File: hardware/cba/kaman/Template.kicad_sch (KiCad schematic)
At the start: 0 parts

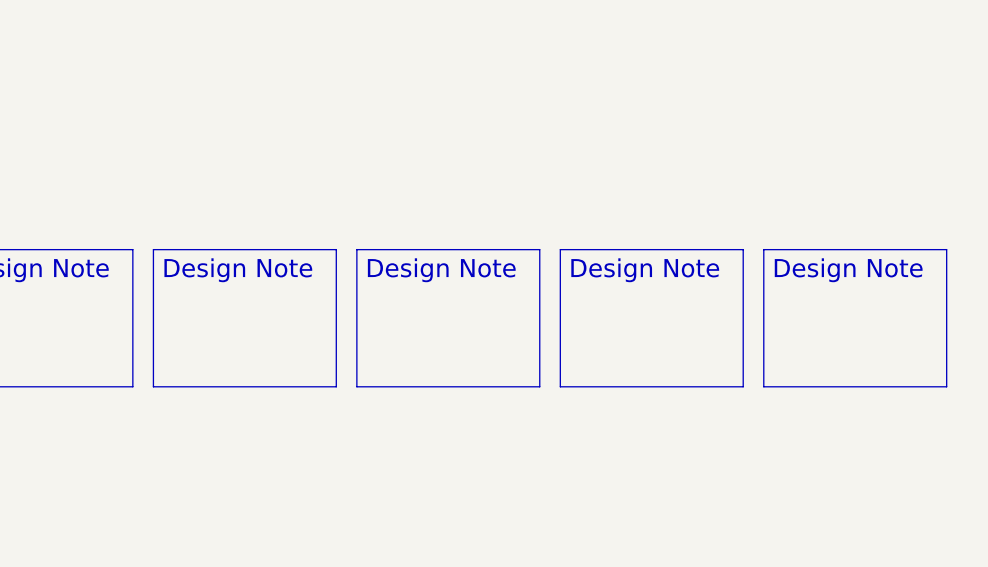
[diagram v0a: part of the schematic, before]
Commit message: hw(schematic): Draw the schematic part of ESP32 C6
Add the ESP32 C6 and it's necessary part's needed for it to function such as the decoupling caps, the auto program circuit and buttons needed
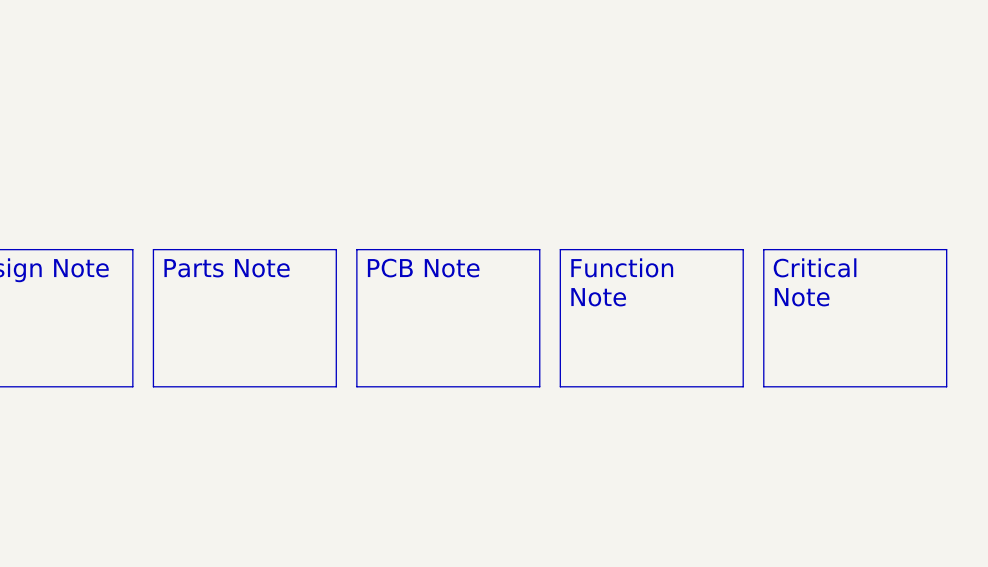
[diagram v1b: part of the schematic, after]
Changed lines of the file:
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@@
 (kicad_sch
-	(version 20250114)
+	(version 20260306)
 	(generator "eeschema")
-	(generator_version "9.0")
+	(generator_version "10.0")
 	(paper "A4")
 	(rectangle
@@
 		)
 	)
-	(text_box "Design Note\n"
+	(text_box "Function Note\n"
 		(exclude_from_sim no)
 		(at 228.6 120.142 0)
@@
 		)
 	)
-	(text_box "Design Note\n"
+	(text_box "Parts Note\n"
 		(exclude_from_sim no)
 		(at 183.388 120.142 0)
@@
 		)
 	)
-	(text_box "Design Note\n"
+	(text_box "PCB Note\n"
 		(exclude_from_sim no)
 		(at 205.994 120.142 0)
@@
 		)
 	)
-	(text_box "Design Note\n"
+	(text_box "Critical Note\n"
 		(exclude_from_sim no)
 		(at 251.206 120.142 0)
@@
 		)
 		(fill
-			(color 0 0 0 0.0000)
+			(color 0 0 0 0)
 		)
 		(property "Sheetname" "Project Architecture"
 			(at 221.488 226.1104 0)
+			(show_name no)
+			(do_not_autoplace no)
 			(effects
 				(font
@@
 		(property "Sheetfile" "project_architecture.kicad_sch"
 			(at 221.488 231.2166 0)
+			(show_name no)
+			(do_not_autoplace no)
 			(effects
 				(font
@@
 		)
 		(instances
-			(project "Driver"
+			(project "Template"
 				(path "/b7abe575-2b7a-4e47-9046-9769d7102f9d"
 					(page "3")
@@
 		)
 		(fill
-			(color 0 0 0 0.0000)
+			(color 0 0 0 0)
 		)
 		(property "Sheetname" "Block Diagram"
 			(at 221.234 217.7284 0)
+			(show_name no)
+			(do_not_autoplace no)
 			(effects
 				(font
@@
 		(property "Sheetfile" "block_diagram.kicad_sch"
 			(at 221.234 222.8346 0)
+			(show_name no)
+			(do_not_autoplace no)
 			(effects
 				(font
@@
 		)
 		(instances
-			(project "Driver"
+			(project "Template"
 				(path "/b7abe575-2b7a-4e47-9046-9769d7102f9d"
 					(page "2")

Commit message: hw(pcb): final 0.2v pcb
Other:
- note added: "0.1"
- note added: "17/6/2026"
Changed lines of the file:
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@@
 		)
 	)
-	(text "Date"
+	(text "17/6/2026"
 		(exclude_from_sim no)
 		(at 257.048 30.48 0)
@@
 		)
 	)
-	(text "Revision Number"
+	(text "0.1"
 		(exclude_from_sim no)
 		(at 179.324 29.972 0)
